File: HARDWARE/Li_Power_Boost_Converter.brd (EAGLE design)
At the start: 26.7 x 12.7 mm, 20 parts, among them U1 TPS61200

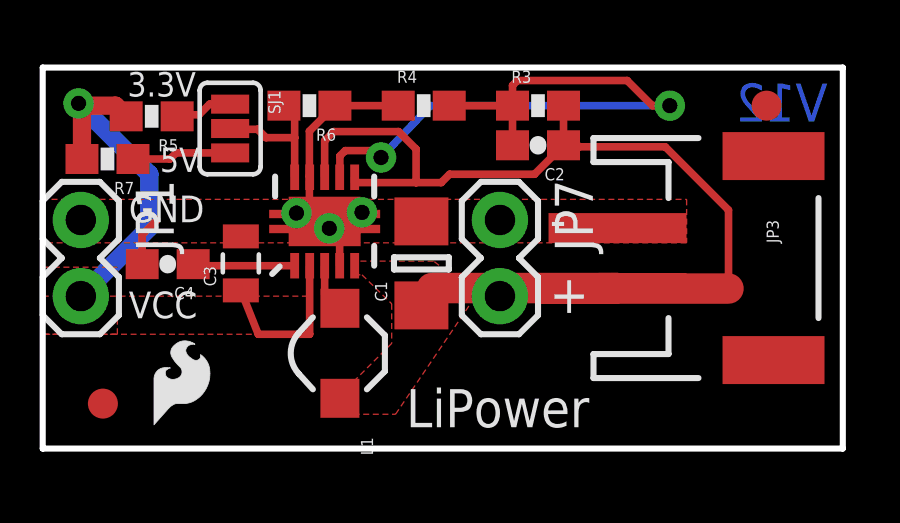
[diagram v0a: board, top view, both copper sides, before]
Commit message: Schematic Cleanup / Heat Sink
Cleaned up a few nets and removed on heat sink for better flow
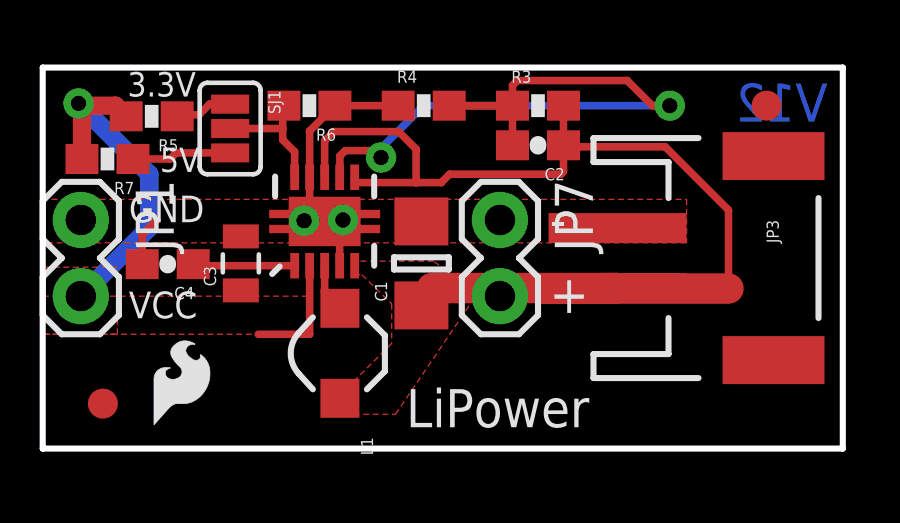
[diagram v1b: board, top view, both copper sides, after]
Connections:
- removed net GND1: R4.1, R6.1, U1.9
- net GND: now also R4.1, R6.1, U1.9
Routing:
- net GND1: track 4.94 -> 0.00 mm
- net GND: track 5.56 -> 9.16 mm, vias 3 -> 2
- net VCC: track 17.5 -> 15.9 mm
- net FB: track 4.89 -> 4.32 mm
- net VIN: track 40.5 -> 41.0 mm
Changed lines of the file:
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@@
 <setting verticaltext="up"/>
 </settings>
-<grid distance="0.05" unitdist="inch" unit="inch" style="lines" multiple="1" display="yes" altdistance="0.001" altunitdist="inch" altunit="inch"/>
+<grid distance="0.05" unitdist="inch" unit="inch" style="lines" multiple="1" display="yes" altdistance="0.005" altunitdist="inch" altunit="inch"/>
 <layers>
 <layer number="1" name="Top" color="4" fill="1" visible="yes" active="yes"/>
@@
 <wire x1="17.8816" y1="10.0584" x2="17.78" y2="10.16" width="0.254" layer="1"/>
 <wire x1="20.7518" y1="10.0584" x2="17.8816" y2="10.0584" width="0.254" layer="1"/>
-<wire x1="13.5636" y1="9.144" x2="16.3948" y2="9.144" width="0.254" layer="1"/>
-<wire x1="16.3948" y1="9.144" x2="17.36" y2="10.1092" width="0.254" layer="1"/>
+<wire x1="13.5636" y1="9.144" x2="17.272" y2="9.144" width="0.254" layer="1"/>
 <wire x1="17.78" y1="10.16" x2="17.4108" y2="10.16" width="0.254" layer="1"/>
 <wire x1="17.4108" y1="10.16" x2="17.36" y2="10.1092" width="0.254" layer="1"/>
@@
 <wire x1="12.446" y1="8.8646" x2="13.2842" y2="8.8646" width="0.254" layer="1"/>
 <wire x1="13.2842" y1="8.8646" x2="13.5636" y2="9.144" width="0.254" layer="1"/>
+<wire x1="17.36" y1="10.1092" x2="17.36" y2="9.232" width="0.254" layer="1"/>
+<wire x1="17.36" y1="9.232" x2="17.272" y2="9.144" width="0.254" layer="1"/>
 </signal>
 <signal name="N$2">
@@
 <wire x1="15.66" y1="11.43" x2="15.66" y2="10.1092" width="0.254" layer="1"/>
 <wire x1="15.66" y1="11.43" x2="13.55" y2="11.43" width="0.254" layer="1"/>
-<wire x1="12.9286" y1="11.43" x2="20.9042" y2="11.43" width="0.254" layer="16"/>
-<wire x1="11.2776" y1="9.7028" x2="12.9286" y2="11.43" width="0.254" layer="16"/>
+<wire x1="12.7" y1="11.43" x2="20.9042" y2="11.43" width="0.254" layer="16"/>
 <via x="11.2776" y="9.7028" extent="1-16" drill="0.508"/>
 <via x="20.9042" y="11.43" extent="1-16" drill="0.508"/>
@@
 <wire x1="10.0838" y1="9.9314" x2="11.049" y2="9.9314" width="0.254" layer="1"/>
 <wire x1="11.049" y1="9.9314" x2="11.2776" y2="9.7028" width="0.254" layer="1"/>
+<wire x1="11.2776" y1="9.7028" x2="11.2776" y2="10.0076" width="0.254" layer="16"/>
+<wire x1="11.2776" y1="10.0076" x2="12.7" y2="11.43" width="0.254" layer="16"/>
 </signal>
 <signal name="FB">
+<contactref element="SJ1" pad="2"/>
+<contactref element="R6" pad="2"/>
 <contactref element="U1" pad="10"/>
-<contactref element="R6" pad="2"/>
-<contactref element="SJ1" pad="2"/>
-<wire x1="8.398" y1="10.3632" x2="8.398" y2="9.0442" width="0.254" layer="1"/>
-<wire x1="8.398" y1="10.3632" x2="8.398" y2="11.272" width="0.254" layer="1"/>
-<wire x1="8.398" y1="11.272" x2="8.04" y2="11.43" width="0.254" layer="1"/>
-<wire x1="6.2484" y1="10.668" x2="6.2738" y2="10.6426" width="0.254" layer="1"/>
-<wire x1="6.2738" y1="10.6426" x2="7.1628" y2="10.6426" width="0.254" layer="1"/>
-<wire x1="7.1628" y1="10.6426" x2="7.4422" y2="10.3632" width="0.254" layer="1"/>
-<wire x1="7.4422" y1="10.3632" x2="8.398" y2="10.3632" width="0.254" layer="1"/>
+<wire x1="8.398" y1="9.0442" x2="8.398" y2="9.89" width="0.254" layer="1"/>
+<wire x1="8.398" y1="9.89" x2="8.001" y2="10.287" width="0.254" layer="1"/>
+<wire x1="8.001" y1="10.668" x2="8.001" y2="11.391" width="0.254" layer="1"/>
+<wire x1="8.001" y1="11.391" x2="8.04" y2="11.43" width="0.254" layer="1"/>
+<wire x1="6.2484" y1="10.668" x2="8.001" y2="10.668" width="0.254" layer="1"/>
+<wire x1="8.001" y1="10.668" x2="8.001" y2="10.287" width="0.254" layer="1"/>
 </signal>
 <signal name="GND">
@@
 <wire x1="9.898" y1="6.0942" x2="9.898" y2="7.358" width="0.254" layer="1"/>
 <wire x1="9.898" y1="7.358" x2="10.16" y2="7.62" width="0.254" layer="1"/>
-<wire x1="9.5504" y1="7.3406" x2="8.898" y2="8.0692" width="0.254" layer="1"/>
-<via x="9.5504" y="7.3406" extent="1-16" drill="0.508"/>
-<via x="8.4582" y="7.8486" extent="1-16" drill="0.508"/>
-<via x="10.6426" y="7.874" extent="1-16" drill="0.508"/>
+<via x="8.7122" y="7.5946" extent="1-16" drill="0.508"/>
+<via x="10.0076" y="7.62" extent="1-16" drill="0.508"/>
 <polygon width="0.2032" layer="1" isolate="0.3048" thermals="no">
 <vertex x="-0.0254" y="8.3058"/>
@@
 <wire x1="3.3156" y1="6.1468" x2="3.3156" y2="7.1256" width="0.254" layer="1"/>
 <wire x1="3.3156" y1="7.1256" x2="3.81" y2="7.62" width="0.254" layer="1"/>
-<wire x1="8.89" y1="8.89" x2="8.89" y2="7.62" width="0.254" layer="1"/>
+<contactref element="U1" pad="9"/>
+<wire x1="8.898" y1="9.0442" x2="8.89" y2="9.0522" width="0.254" layer="1"/>
+<wire x1="8.89" y1="8.0772" x2="8.898" y2="8.0692" width="0.254" layer="1"/>
+<wire x1="8.898" y1="9.0442" x2="8.898" y2="8.0852" width="0.254" layer="1"/>
+<wire x1="8.898" y1="8.0852" x2="8.89" y2="8.0772" width="0.254" layer="1"/>
+<wire x1="8.898" y1="9.0442" x2="8.898" y2="10.572" width="0.254" layer="1"/>
+<wire x1="8.898" y1="10.572" x2="8.89" y2="10.58" width="0.254" layer="1"/>
+<contactref element="R4" pad="1"/>
+<contactref element="R6" pad="1"/>
+<wire x1="11.85" y1="11.43" x2="9.74" y2="11.43" width="0.254" layer="1"/>
+<wire x1="8.898" y1="10.572" x2="8.898" y2="10.588" width="0.254" layer="1"/>
+<wire x1="8.898" y1="10.588" x2="9.74" y2="11.43" width="0.254" layer="1"/>
 </signal>
 <signal name="3.3V">
@@
 <wire x1="8.89" y1="3.81" x2="8.898" y2="3.818" width="0.254" layer="1"/>
 <wire x1="7.1852" y1="3.81" x2="8.89" y2="3.81" width="0.254" layer="1"/>
-<wire x1="7.1852" y1="3.81" x2="6.604" y2="5.2722" width="0.254" layer="1"/>
 <wire x1="1.27" y1="5.08" x2="3.556" y2="7.366" width="0.6096" layer="16"/>
 <wire x1="3.556" y1="7.366" x2="3.556" y2="9.144" width="0.6096" layer="16"/>
@@
 <wire x1="2.4266" y1="11.43" x2="1.27" y2="11.43" width="0.6096" layer="1"/>
 </signal>
-<signal name="GND1">
-<contactref element="U1" pad="9"/>
-<contactref element="R4" pad="1"/>
-<contactref element="R6" pad="1"/>
-<wire x1="8.898" y1="9.0442" x2="8.89" y2="9.0522" width="0.254" layer="1"/>
-<wire x1="9.74" y1="11.43" x2="11.85" y2="11.43" width="0.254" layer="1"/>
-<wire x1="8.89" y1="9.0522" x2="8.9154" y2="9.0776" width="0.254" layer="1"/>
-<wire x1="9.74" y1="11.3656" x2="9.74" y2="11.43" width="0.254" layer="1"/>
-<wire x1="8.9154" y1="9.0776" x2="8.89" y2="9.103" width="0.254" layer="1"/>
-<wire x1="8.89" y1="9.103" x2="8.89" y2="10.58" width="0.254" layer="1"/>
-<wire x1="8.89" y1="10.58" x2="9.74" y2="11.43" width="0.254" layer="1"/>
-</signal>
 </signals>
-<errors>
-</errors>
 </board>
 </drawing>

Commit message: Trace Work
Routed all traces away from the Microcontroller, did a little trace
cleanup as well.
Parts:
- removed U$1: CREATIVE_COMMONS, SparkFun:CREATIVE_COMMONS
- added FRAME1: FRAME-LETTER, SparkFun-Aesthetics:CREATIVE_COMMONS
- added U$2: (no value), SparkFun-Aesthetics:OSHW-LOGO-S
- moved JP6 4.40 mm to (23.0, 3.89)
- moved R6 0.13 mm to (8.92, 11.6)
- moved C2 0.10 mm to (16.5, 10.0)
- moved R4 0.10 mm to (12.7, 11.5)
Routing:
- net VIN: track 41.0 -> 42.8 mm
- net N$1: track 3.40 -> 4.69 mm
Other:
- board text added: "Aaron Weiss Sparkfun.com"
- board text added: "Oleg Mazurov circuitsathome.com"

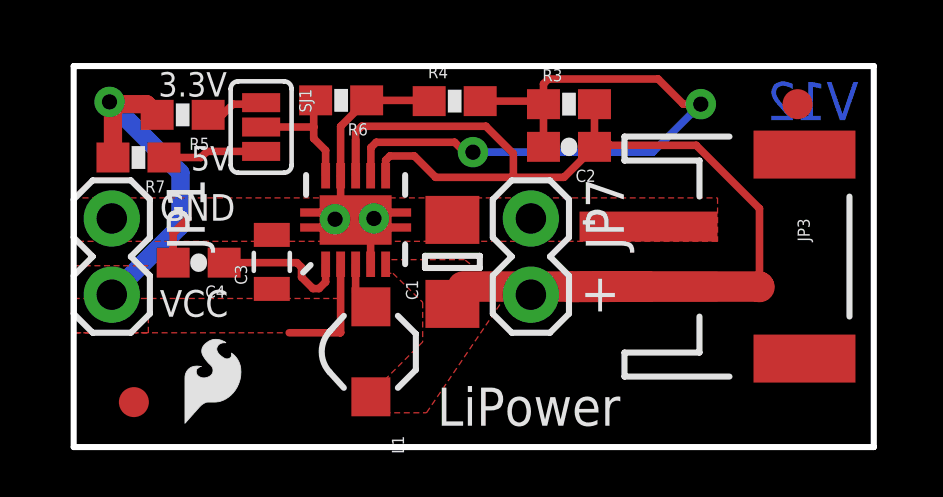
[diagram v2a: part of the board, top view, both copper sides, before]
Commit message: Res/Cap Spacing
Some of the res/caps needed some moving as well as the jumper.  Moved
them and re routed accordingly .
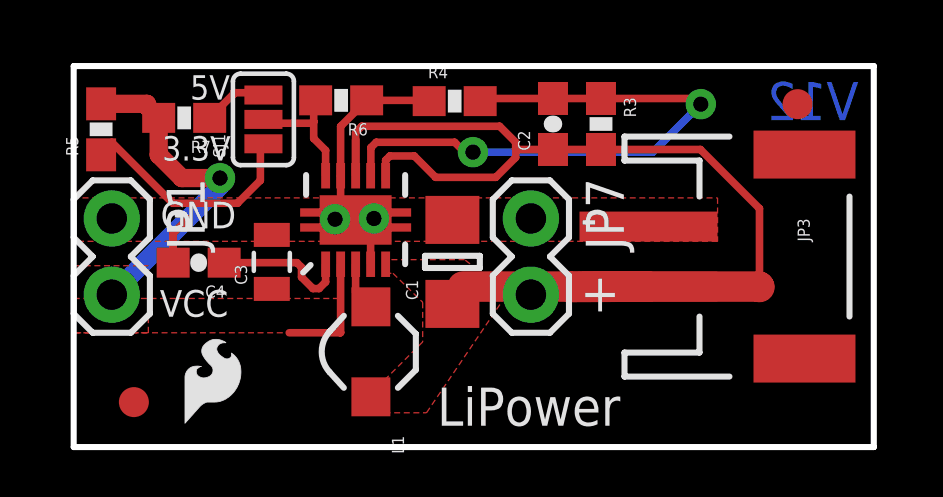
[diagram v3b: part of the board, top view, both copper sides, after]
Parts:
- moved JP6 5.21 mm to (19.4, 0.21)
- moved R5 2.76 mm to (0.91, 10.6), turned to 90 degrees
- moved R7 2.02 mm to (3.68, 11.0)
- moved R3 1.25 mm to (17.6, 10.8), turned to 270 degrees
- moved C2 0.93 mm to (16.0, 10.8), turned to 90 degrees
- moved SJ1 0.27 mm to (6.32, 10.9), turned to 90 degrees
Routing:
- net 3.3V: track 1.93 -> 7.94 mm
- net UVLO: track 22.9 -> 20.3 mm
- net VIN: track 42.8 -> 40.2 mm
- net 5V: track 3.32 -> 2.19 mm
- net VCC: track 15.9 -> 15.1 mm
